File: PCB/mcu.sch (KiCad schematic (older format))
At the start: 58 parts, among them P1 USB_CONN, P11 2PIN, P12 2PIN, P13 2PIN, P15 2PIN, P2 USB3, P3 USB3_MICRO, P4 6PIN, P5 6PIN, P6 ISP6, P7_1 5PIN, P7_2 5PIN, U1 Atmega32u4, U2 MCP23018, U3 IP4234CZ6, U4 74HC138, U5 PAM2804, X1 CRYSTAL

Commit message: Updating schematic to use STM32F303CC microcontroller instead of ATMEGA32U4; next steps: swapping out USB3 interconnect for HDMI.
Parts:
- removed C14: 8pF, prettylib:SMD_0805, symbol C
- removed C2: 1uF, prettylib:SMD_0805, symbol C
- removed C3, C4, C5, C7, C9: 0.1uF, prettylib:SMD_0805, symbol C
- removed JP1: JUMPER, prettylib:JUMPER_SMD_3, symbol JUMPER3
- removed P6: ISP6, prettylib:TC2030_BIG, symbol ISP6
- removed R5, R6: 2.2k, prettylib:SMD_0805, symbol R
- removed R9: 10k, prettylib:SMD_0805, symbol R
- removed U1: Atmega32u4, prettylib:TQFP44, symbol Atmega32u4
- removed U4: 74HC138, prettylib:SO-16-N, symbol 74HC138
- removed X1: CRYSTAL, prettylib:NX3225SA, symbol CRYSTAL
- added C2: 22uF, prettylib:SMD_0805, symbol Device:CP
- added C3: 22pF, prettylib:SMD_0805, symbol TS65-rescue:C
- added C4, C5, C7, C9: 0.1uF, prettylib:SMD_0805, symbol TS65-rescue:C
- added J1: Programming, Connector_PinHeader_2.54mm:PinHeader_1x04_P2.54mm_Vertical, symbol Connector_Generic:Conn_01x04
- added Q1: NTR1P02T1G - PMOS, prettylib:SOT-23, symbol Device:Q_PMOS_GSD
- added R1: 1.5k, prettylib:SMD_0805, symbol TS65-rescue:R
- added R2, R8, R9: 10k, prettylib:SMD_0805, symbol TS65-rescue:R
- added R5, R6: 2.2k, prettylib:SMD_0805, symbol TS65-rescue:R
- added R7: 100k, prettylib:SMD_0805, symbol TS65-rescue:R
- added S3: TAC_SWITCH, prettylib:TACT_5.2x5.2, symbol TS65-rescue:TAC_SWITCH
- added U6: AP1117-33, Package_TO_SOT_SMD:SOT-223-3_TabPin2, symbol Regulator_Linear:AP1117-33
- added U7: STM32F303CCTx, Package_QFP:LQFP-48_7x7mm_P0.5mm, symbol MCU_ST_STM32F3:STM32F303CCTx
- added Y1: 8M ABM2-8.000MHZ-D4Y-T, prettylib:ABRACON-ABM2_xtal, symbol Device:Crystal
- BZ1: symbol SPEAKER -> TS65-rescue:SPEAKER
- C1, C10, C11, C12, C17, C18: symbol CT -> TS65-rescue:CT
- C13: value 8pF -> 22pF; symbol C -> TS65-rescue:C
- C20_1, C20_2, C6, C8: symbol C -> TS65-rescue:C
- F1: symbol FUSE -> TS65-rescue:FUSE
- L2: symbol INDUCTOR -> TS65-rescue:INDUCTOR
- P1: symbol USB_CONN -> TS65-rescue:USB_CONN
- P11, P12, P13, P15: symbol 2PIN -> TS65-rescue:2PIN
- P2: symbol USB3 -> TS65-rescue:USB3
- P3: symbol USB3_MICRO -> TS65-rescue:USB3_MICRO
- P4, P5: symbol 6PIN -> TS65-rescue:6PIN
- P7_1, P7_2: symbol 5PIN -> TS65-rescue:5PIN
- R13_1, R13_2, R14, R25, R28_1, R28_2, R3, R31_1, R31_2, R33, R4, R71, R72: symbol R -> TS65-rescue:R
- S1: symbol TAC_SWITCH -> TS65-rescue:TAC_SWITCH
- S2: symbol ENCODER -> TS65-rescue:ENCODER
- U2: symbol MCP23018_SSOP -> TS65-rescue:MCP23018_SSOP
- U3: symbol IP4234CZ6 -> TS65-rescue:IP4234CZ6
- U5: symbol PAM2804 -> TS65-rescue:PAM2804
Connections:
- net +5V: now also Q1.2 (S), U6.3 (VI); no longer C6.1, P2.1, P3.1, P5.1, R14.2, R71.2, R72.1, U2.10 (VCC), U2.14 (RESET)
- net BUZZER: now also U7.12 (PA2)
- net COL1: now also U7.2 (PC13)
- net COL2: now also U7.3 (PC14)
- net COL3: now also U7.4 (PC15)
- net COL4: now also U7.18 (PB0)
- net COL5: now also U7.19 (PB1)
- net COL6: now also U7.20 (PB2)
- net COL7: now also U7.39 (PB3)
- net ENCA: now also U7.41 (PB5)
- net ENCB: now also U7.40 (PB4)
- net LEDBL: now also U7.27 (PB14)
- net LEDCL: now also U7.15 (PA5)
- net LEDI1: now also U7.16 (PA6)
- net LEDI2: now also U7.17 (PA7)
- net LEDI3: now also U7.14 (PA4)
- net LEDI4: now also U7.29 (PA8)
- net MCURST: now also U7.7 (NRST)
- net RGBLDIN: now also U7.28 (PB15), U7.45 (PB8)
- net ROWL1: now also U7.21 (PB10)
- net ROWL2: now also U7.22 (PB11); no longer P4.3
- net ROWL3: now also U7.25 (PB12); no longer P4.2
- net ROWL4: now also U7.26 (PB13); no longer P4.1
- net ROWL5: now also U7.46 (PB9)
- net RX: now also U7.31 (PA10)
- net SCL: now also R6.2, U7.42 (PB6)
- net SDA: now also R5.2, U7.43 (PB7)
- net TPCLK: now also U7.10 (PA0)
- net TPDATA: now also U7.11 (PA1)
- net TX: now also U7.30 (PA9)
- net USB_D+: now also R1.1, U7.33 (PA12)
- net USB_D-: now also U7.32 (PA11)
- net VSS: now also C2.2, C3.2, C4.1, C5.1, C7.1, C9.1, J1.4 (Pin_4), R2.1, R7.2, R9.2, U6.1 (GND), U7.23 (VSS), U7.35 (VSS), U7.47 (VSS), U7.8 (VSSA)
- net XTAL1: now also C3.1, U7.5 (PF0), Y1.2
- net XTAL2: now also U7.6 (PF1), Y1.1
- new net: Q1.3 (D), R1.2
- new net +3V3: C2.1, C4.2, C5.2, C6.1, C7.2, C9.2, J1.1 (Pin_1), P2.1, P3.1, P5.1, R14.2, R5.1, R6.1, R71.2, R72.1, R8.2, S3.3, S3.4, U2.10 (VCC), U2.14 (RESET), U6.2 (VO), U7.1 (VBAT), U7.24 (VDD), U7.36 (VDD), U7.48 (VDD), U7.9 (VDDA)
- new net BOOT0: R7.1, S3.2, U7.44 (BOOT0)
- new net MISO: P4.1
- new net MOSI: P4.2
- new net SCLK: P4.3
- new net SWCLK: J1.3 (Pin_3), R8.1, U7.37 (PA14)
- new net SWDIO: J1.2 (Pin_2), R9.1, U7.34 (PA13)
- new net USB_RESET: Q1.1 (G), R2.2, U7.13 (PA3)
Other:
- note added: "BOOT0"
- note added: "Programming"
- note added: "Voltage Regulator"
- note removed: "Decoupling capacitors"
- note removed: "HWBE Jumper"
- note removed: "I2C Pullups"
- note removed: "ISP Tag Connect"
- moved on the sheet: C1, C12, F1, P1, R3, R4, U3

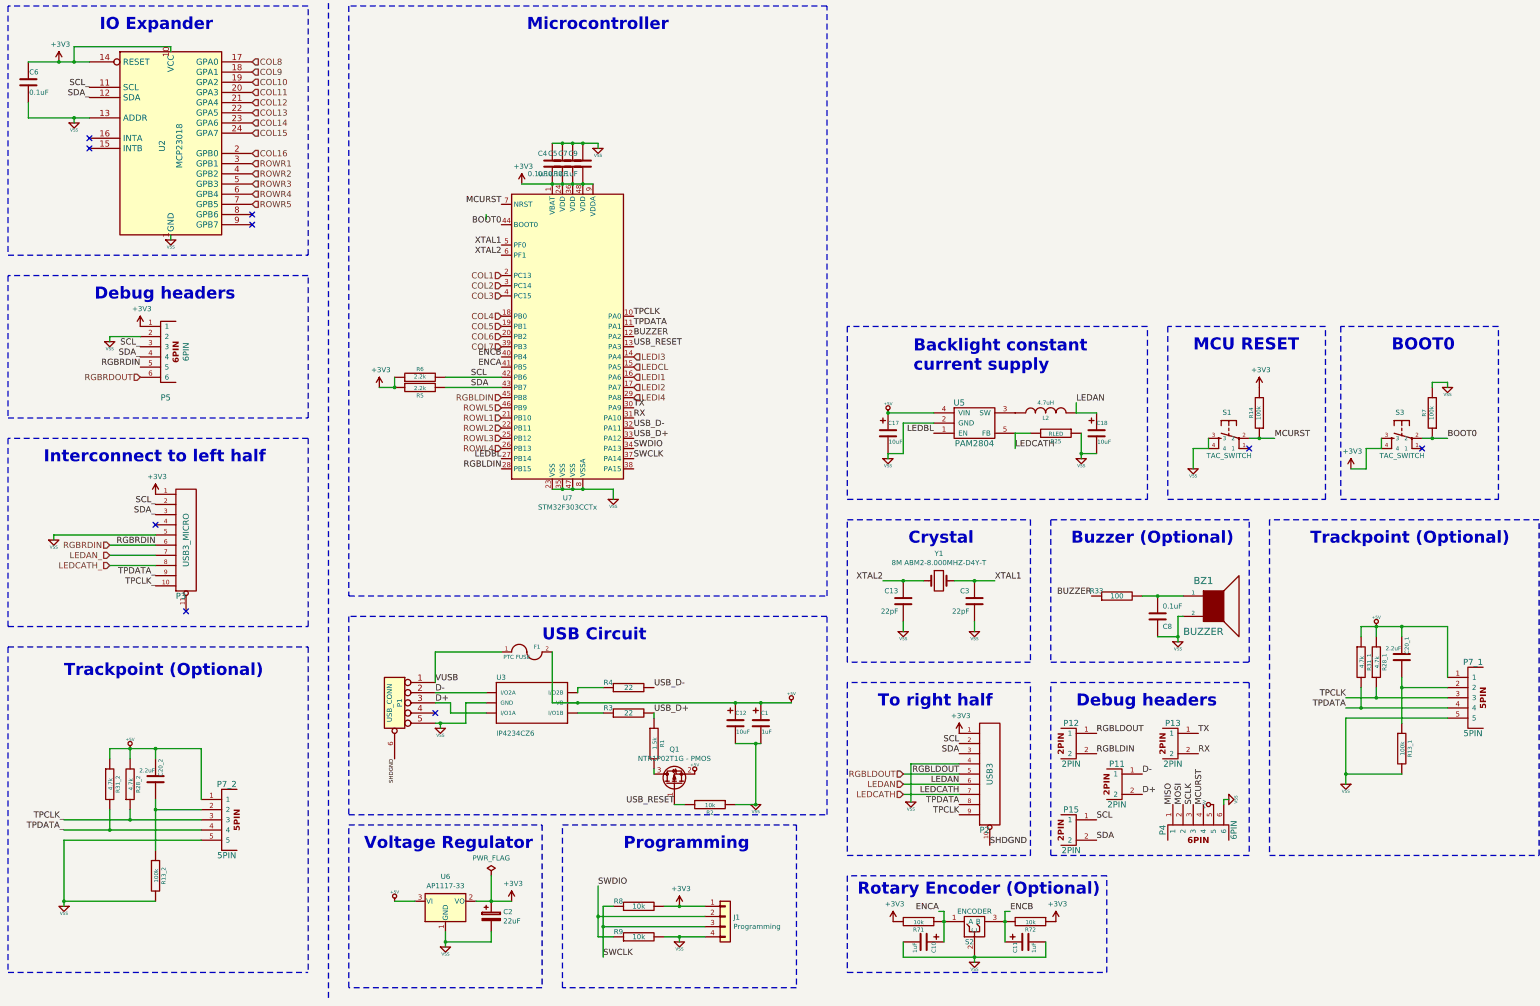
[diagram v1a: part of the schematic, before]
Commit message: Updating design to use STM32F303 instead of AVR32u4.
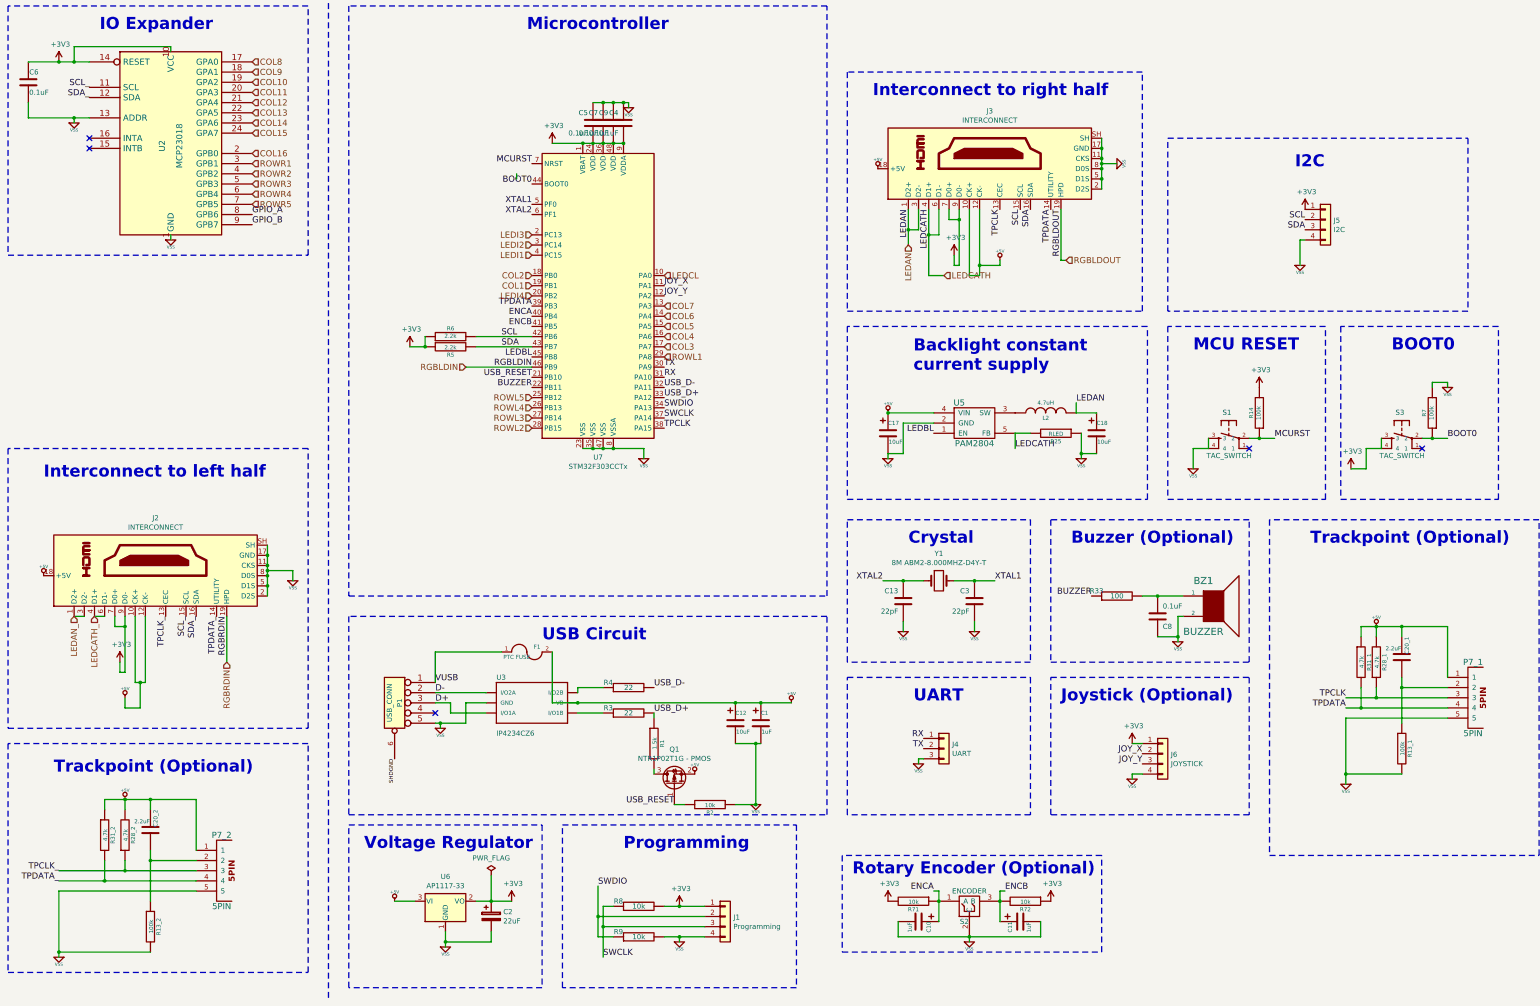
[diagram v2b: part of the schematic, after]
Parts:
- removed P11, P12, P13, P15: 2PIN, prettylib:Pin_Header_1x02, symbol TS65-rescue:2PIN
- removed P2: USB3, prettylib:USB3_AFEMALE_MOD, symbol TS65-rescue:USB3
- removed P3: USB3_MICRO, prettylib:USB3_MICROB, symbol TS65-rescue:USB3_MICRO
- removed P4, P5: 6PIN, prettylib:Pin_Header_1x06, symbol TS65-rescue:6PIN
- added J2, J3: INTERCONNECT, prettylib:47151-0001, symbol Connector:HDMI_A
- added J4: UART, Connector_PinHeader_2.54mm:PinHeader_1x03_P2.54mm_Vertical, symbol Connector_Generic:Conn_01x03
- added J5: I2C, Connector_PinHeader_2.54mm:PinHeader_1x04_P2.54mm_Vertical, symbol Connector_Generic:Conn_01x04
- added J6: JOYSTICK, Connector_PinHeader_2.54mm:PinHeader_1x04_P2.54mm_Vertical, symbol Connector_Generic:Conn_01x04
- C2: footprint prettylib:SMD_0805 -> Resistor_SMD:R_1206_3216Metric
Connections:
- net +3V3: now also J2.7 (D0+), J2.9 (D0-), J3.7 (D0+), J3.9 (D0-), J5.1 (Pin_1), J6.1 (Pin_1)
- net +5V: now also J2.10 (CK+), J2.12 (CK-), J2.18 (+5V), J3.10 (CK+), J3.12 (CK-), J3.18 (+5V)
- net BUZZER: now also U7.22 (PB11); no longer U7.12 (PA2)
- net COL1: now also U7.19 (PB1); no longer U7.2 (PC13)
- net COL2: now also U7.18 (PB0); no longer U7.3 (PC14)
- net COL3: now also U7.17 (PA7); no longer U7.4 (PC15)
- net COL4: now also U7.16 (PA6); no longer U7.18 (PB0)
- net COL5: now also U7.15 (PA5); no longer U7.19 (PB1)
- net COL6: now also U7.14 (PA4); no longer U7.20 (PB2)
- net COL7: now also U7.13 (PA3); no longer U7.39 (PB3)
- net ENCA: now also U7.40 (PB4); no longer U7.41 (PB5)
- net ENCB: now also U7.41 (PB5); no longer U7.40 (PB4)
- net LEDAN: now also J3.1 (D2+), J3.3 (D2-)
- net LEDAN_: now also J2.1 (D2+), J2.3 (D2-)
- net LEDBL: now also U7.45 (PB8); no longer U7.27 (PB14)
- net LEDCATH: now also J3.4 (D1+), J3.6 (D1-)
- net LEDCATH_: now also J2.4 (D1+), J2.6 (D1-)
- net LEDCL: now also U7.10 (PA0); no longer U7.15 (PA5)
- net LEDI1: now also U7.4 (PC15); no longer U7.16 (PA6)
- net LEDI2: now also U7.3 (PC14); no longer U7.17 (PA7)
- net LEDI3: now also U7.2 (PC13); no longer U7.14 (PA4)
- net LEDI4: now also U7.20 (PB2); no longer U7.29 (PA8)
- net RGBLDIN: now also U7.46 (PB9); no longer U7.28 (PB15), U7.45 (PB8)
- net RGBLDOUT: now also J3.19 (HPD)
- net RGBRDIN: now also J2.19 (HPD)
- net ROWL1: now also U7.29 (PA8); no longer U7.21 (PB10)
- net ROWL2: now also U7.28 (PB15); no longer U7.22 (PB11)
- net ROWL3: now also U7.27 (PB14); no longer U7.25 (PB12)
- net ROWL5: now also U7.25 (PB12); no longer U7.46 (PB9)
- net RX: now also J4.1 (Pin_1)
- net SCL: now also J3.15 (SCL), J5.2 (Pin_2)
- net SCL_: now also J2.15 (SCL)
- net SDA: now also J3.16 (SDA), J5.3 (Pin_3)
- net SDA_: now also J2.16 (SDA)
- net TPCLK: now also U7.38 (PA15), J3.13 (CEC); no longer U7.10 (PA0)
- net TPCLK_: now also J2.13 (CEC)
- net TPDATA: now also U7.39 (PB3), J3.14 (UTILITY); no longer U7.11 (PA1)
- net TPDATA_: now also J2.14 (UTILITY)
- net TX: now also J4.2 (Pin_2)
- net USB_RESET: now also U7.21 (PB10); no longer U7.13 (PA3)
- net VSS: now also J2.11 (CKS), J2.17 (GND), J2.2 (D2S), J2.5 (D1S), J2.8 (D0S), J2.SH, J3.11 (CKS), J3.17 (GND), J3.2 (D2S), J3.5 (D1S), J3.8 (D0S), J3.SH, J4.3 (Pin_3), J5.4 (Pin_4), J6.4 (Pin_4)
- net GPIO_A: now reaches U2.8 (GPB6)
- net GPIO_B: now reaches U2.9 (GPB7)
- new net JOY_X: J6.2 (Pin_2), U7.11 (PA1)
- new net JOY_Y: J6.3 (Pin_3), U7.12 (PA2)
- no-connect marks 9 -> 5
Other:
- note added: "I2C"
- note added: "Interconnect to right half"
- note added: "Joystick (Optional)"
- note added: "UART"
- note removed: "Debug headers"
- note removed: "To right half"
- moved on the sheet: C10, C11, C20_2, C4, C5, C7, C9, P7_2, R13_2, R28_2, R31_2, R5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

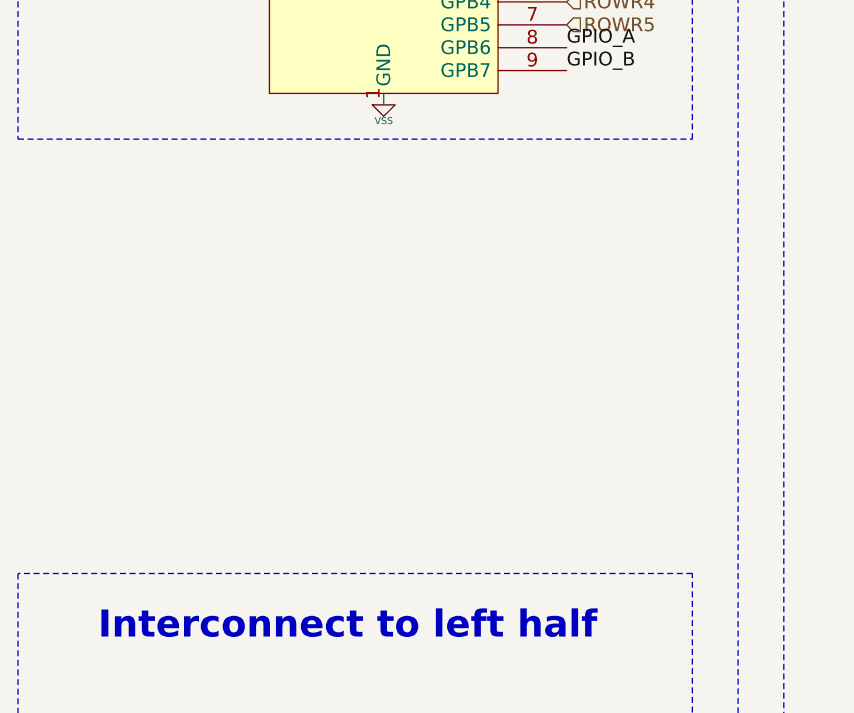
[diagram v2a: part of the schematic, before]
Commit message: Updating to re-include expansion port from left side.
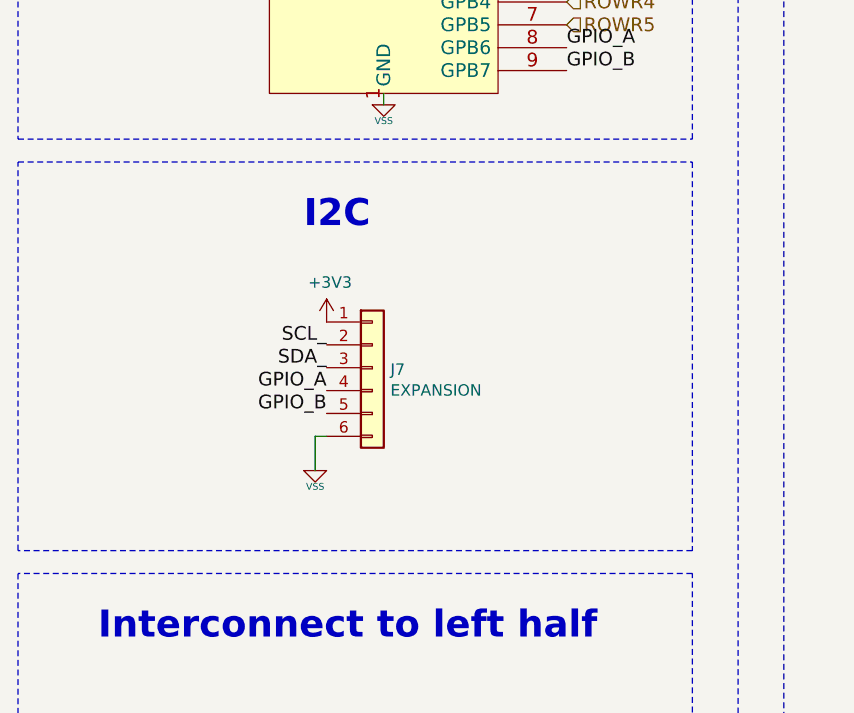
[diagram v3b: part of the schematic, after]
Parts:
- added J7: EXPANSION, Connector_PinHeader_2.54mm:PinHeader_1x06_P2.54mm_Vertical, symbol Connector_Generic:Conn_01x06
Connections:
- net +3V3: now also J7.1 (Pin_1)
- net GPIO_A: now also J7.4 (Pin_4)
- net GPIO_B: now also J7.5 (Pin_5)
- net SCL_: now also J7.2 (Pin_2)
- net SDA_: now also J7.3 (Pin_3)
- net VSS: now also J7.6 (Pin_6)
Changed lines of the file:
@@
 Wire Wire Line
 	13450 3700 13450 3950
+$Comp
+L power:+3V3 #PWR0132
+U 1 1 5BACBDC0
+P 2100 4650
+F 0 "#PWR0132" H 2100 4500 50  0001 C CNN
+F 1 "+3V3" H 2115 4823 50  0000 C CNN
+F 2 "" H 2100 4650 50  0001 C CNN
+F 3 "" H 2100 4650 50  0001 C CNN
+	1    2100 4650
+	1    0    0    -1
+$EndComp
+$Comp
+L TS65-rescue:VSS #PWR0133
+U 1 1 5BACBDC6
+P 2050 5300
+F 0 "#PWR0133" H 2050 5300 30  0001 C CNN
+F 1 "VSS" H 2050 5230 30  0000 C CNN
+F 2 "" H 2050 5300 60  0001 C CNN
+F 3 "" H 2050 5300 60  0001 C CNN
+	1    2050 5300
+	1    0    0    -1
+$EndComp
+Text Label 2100 4750 2    60   ~ 0
+SCL_
+Text Label 2100 4850 2    60   ~ 0
+SDA_
+Text Notes 2000 4250 0    118  ~ 24
+I2C
+Wire Notes Line
+	750  3950 3700 3950
+Wire Notes Line
+	3700 3950 3700 5650
+Wire Notes Line
+	3700 5650 750  5650
+Wire Notes Line
+	750  5650 750  3950
+$Comp
+L Connector_Generic:Conn_01x06 J7
+U 1 1 5BADDCE1
+P 2300 4850
+F 0 "J7" H 2379 4842 50  0000 L CNN
+F 1 "EXPANSION" H 2379 4751 50  0000 L CNN
+F 2 "Connector_PinHeader_2.54mm:PinHeader_1x06_P2.54mm_Vertical" H 2300 4850 50  0001 C CNN
+F 3 "~" H 2300 4850 50  0001 C CNN
+	1    2300 4850
+	1    0    0    -1
+$EndComp
+Wire Wire Line
+	2100 5150 2050 5150
+Wire Wire Line
+	2050 5150 2050 5300
+Text Label 2100 4950 2    60   ~ 0
+GPIO_A
+Text Label 2100 5050 2    60   ~ 0
+GPIO_B
 $EndSCHEMATC
